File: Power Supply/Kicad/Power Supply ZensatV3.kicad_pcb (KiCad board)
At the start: 2 copper layers, 7 parts, among them J1 ZenBus, Q1 QM6006D, U1 INA3221, U2 INA3221, U3 STM32L476RGTx, U4 LMR33640DDDA, U5 LMR33640DDDA

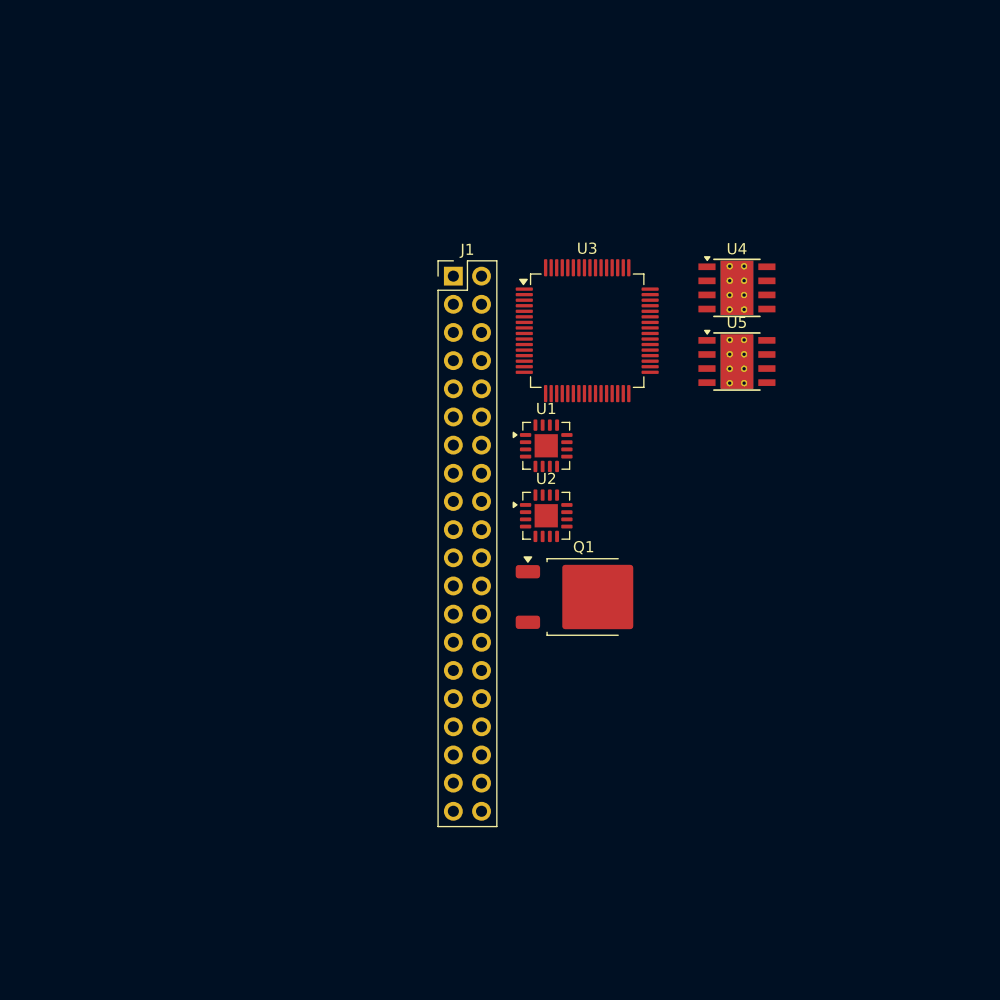
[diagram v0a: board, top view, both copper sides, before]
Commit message: Mais adição
Conclusão do esquema dos reguladores e [início da] organização do esquema.
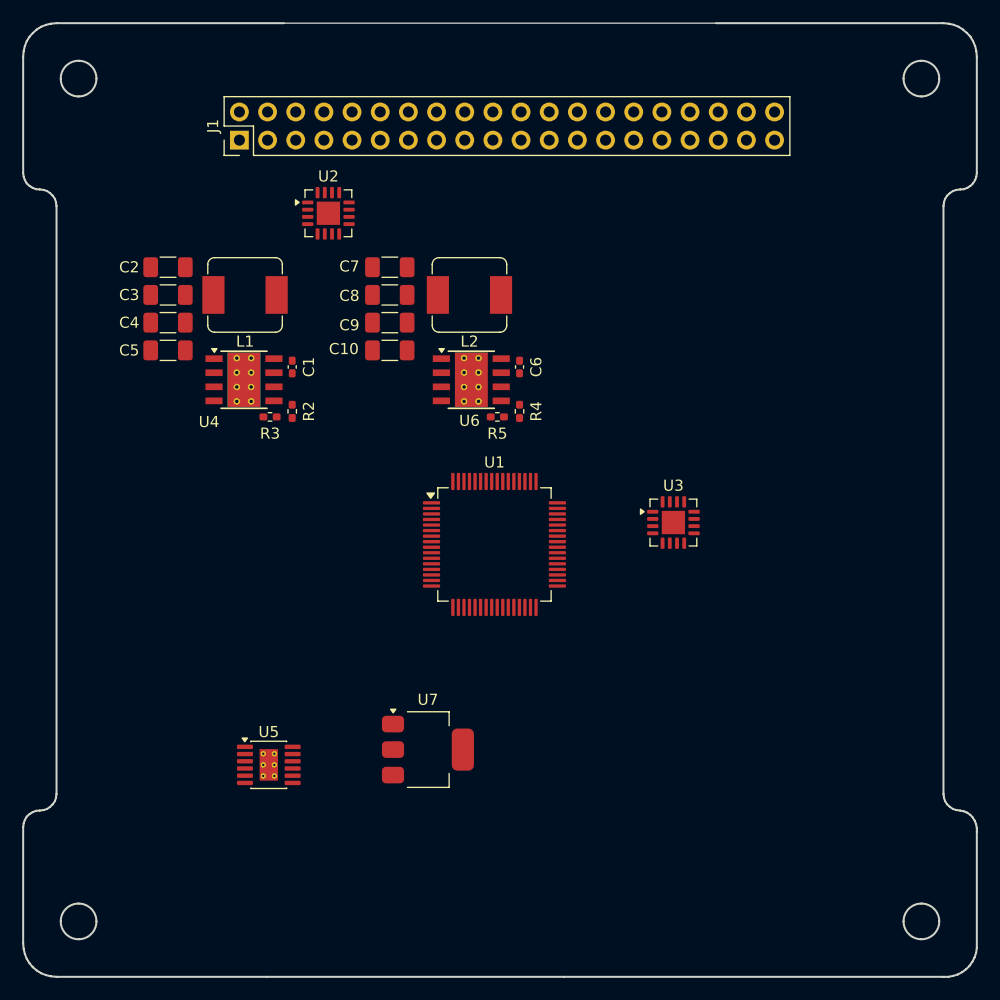
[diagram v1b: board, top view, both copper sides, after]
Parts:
- removed Q1: QM6006D, Package_TO_SOT_SMD:TO-252-2
- added C1: 100nF, Capacitor_SMD:C_0402_1005Metric_Pad0.74x0.62mm_HandSolder, F.Cu at (126.8, 85.0)
- added C10: 22uF, Capacitor_SMD:C_1206_3216Metric_Pad1.33x1.80mm_HandSolder, F.Cu at (135.6, 83.5)
- added C2: 22uF, Capacitor_SMD:C_1206_3216Metric_Pad1.33x1.80mm_HandSolder, F.Cu at (115.6, 76.0)
- added C3: 22uF, Capacitor_SMD:C_1206_3216Metric_Pad1.33x1.80mm_HandSolder, F.Cu at (115.6, 78.5)
- added C4: 22uF, Capacitor_SMD:C_1206_3216Metric_Pad1.33x1.80mm_HandSolder, F.Cu at (115.6, 81.0)
- added C5: 22uF, Capacitor_SMD:C_1206_3216Metric_Pad1.33x1.80mm_HandSolder, F.Cu at (115.6, 83.5)
- added C6: 100nF, Capacitor_SMD:C_0402_1005Metric_Pad0.74x0.62mm_HandSolder, F.Cu at (147.3, 85.0)
- added C7: 22uF, Capacitor_SMD:C_1206_3216Metric_Pad1.33x1.80mm_HandSolder, F.Cu at (135.6, 76.0)
- added C8: 22uF, Capacitor_SMD:C_1206_3216Metric_Pad1.33x1.80mm_HandSolder, F.Cu at (135.6, 78.5)
- added C9: 22uF, Capacitor_SMD:C_1206_3216Metric_Pad1.33x1.80mm_HandSolder, F.Cu at (135.6, 81.0)
- added L1: 6,8uH, Inductor_SMD:L_Sumida_CDMC6D28_7.25x6.5mm, F.Cu at (122.5, 78.5)
- added L2: 8uH, Inductor_SMD:L_Sumida_CDMC6D28_7.25x6.5mm, F.Cu at (142.7, 78.5)
- added R2: R_Small, Resistor_SMD:R_0402_1005Metric_Pad0.72x0.64mm_HandSolder, F.Cu at (126.8, 89.0)
- added R3: R_Small, Resistor_SMD:R_0402_1005Metric_Pad0.72x0.64mm_HandSolder, F.Cu at (124.8, 89.5)
- added R4: R_Small, Resistor_SMD:R_0402_1005Metric_Pad0.72x0.64mm_HandSolder, F.Cu at (147.3, 89.0)
- added R5: R_Small, Resistor_SMD:R_0402_1005Metric_Pad0.72x0.64mm_HandSolder, F.Cu at (145.3, 89.5)
- added U6: LMR33630ADDA, Package_SO:Texas_HSOP-8-1EP_3.9x4.9mm_P1.27mm_ThermalVias, F.Cu at (142.9, 86.2)
- added U7: AMS1117-3.3, Package_TO_SOT_SMD:SOT-223-3_TabPin2, F.Cu at (139.0, 119.5)
- U1: value INA3221 -> STM32L476RGTx; footprint Package_DFN_QFN:Texas_RGV0016A_VQFN-16-1EP_4x4mm_P0.65mm_EP2.1x2.1mm -> Package_QFP:LQFP-64_10x10mm_P0.5mm
- U3: value STM32L476RGTx -> INA3221; footprint Package_QFP:LQFP-64_10x10mm_P0.5mm -> Package_DFN_QFN:Texas_RGV0016A_VQFN-16-1EP_4x4mm_P0.65mm_EP2.1x2.1mm
- U4: value LMR33640DDDA -> LMR33630ADDA
- U5: value LMR33640DDDA -> LT3652IMSE; footprint Package_SO:Texas_HSOP-8-1EP_3.9x4.9mm_P1.27mm_ThermalVias -> Package_SO:MSOP-12-1EP_3x4.039mm_P0.65mm_EP1.651x2.845mm_ThermalVias
- moved U5 55.7 mm to (124.7, 120.9)
- moved U4 45.2 mm to (122.4, 86.2)
- moved U2 33.6 mm to (130.0, 71.1)
- moved J1 22.9 mm to (122.0, 64.5), turned to 90 degrees
- moved U3 19.0 mm to (161.1, 99.0)
- moved U1 10.0 mm to (145.0, 101.0)
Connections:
- net /3V3 renamed /Main PCB/3V3
- net /5V renamed /Main PCB/5V
- net /BAT+ renamed /Main PCB/BAT+
- net /CAN_H renamed /Main PCB/CAN_H
- net /CAN_L renamed /Main PCB/CAN_L
- net /MISO renamed /Main PCB/MISO
- net /MOSI renamed /Main PCB/MOSI
- net /SCL renamed /Main PCB/SCL
- net /SCLK renamed /Main PCB/SCLK
- net /SDA renamed /Main PCB/SDA
- net /SOL+ renamed /Main PCB/SOL+
- net /SOL- renamed /Main PCB/SOL-
- U1 pad 12: unconnected-(U1-IN+1-Pad12) -> GND
- U1 pad 3: GND -> unconnected-(U1-PC14-Pad3)
- U3 pad 12: GND -> unconnected-(U3-IN+1-Pad12)
- U3 pad 3: unconnected-(U3-PC14-Pad3) -> GND
- U4 pad 1: Net-(U4-GND-Pad1) -> GND
- U4 pad 2: unconnected-(U4-VIN-Pad2) -> /Regulators/BAT+
- U4 pad 3: unconnected-(U4-EN-Pad3) -> /Regulators/BAT+
- U4 pad 5: unconnected-(U4-FB-Pad5) -> Net-(U4-FB)
- U4 pad 7: unconnected-(U4-BOOT-Pad7) -> Net-(U4-BOOT)
- U4 pad 8: unconnected-(U4-SW-Pad8) -> Net-(U4-SW)
- U4 pad 9: Net-(U4-GND-Pad1) -> GND
- U5 pad 1: Net-(U5-GND-Pad1) -> unconnected-(U5-V_{IN}-Pad1)
- U5 pad 9: Net-(U5-GND-Pad1) -> unconnected-(U5-BAT-Pad9)
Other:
- board outline added: 86 x 86 mm
